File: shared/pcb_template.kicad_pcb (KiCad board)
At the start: 2 copper layers, 100 x 50 mm, 8 parts, among them J1 WEST TOP, J2 WEST BOT, J3 EAST TOP, J4 EAST BOT, X2 HOLE, X3 HOLE, X4 HOLE, X5 HOLE

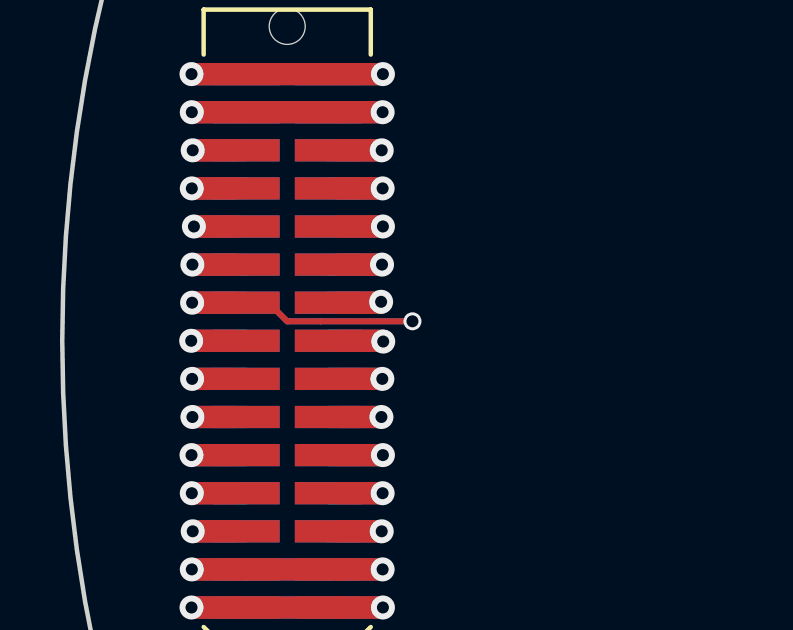
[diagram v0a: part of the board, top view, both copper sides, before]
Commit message: added pcb template
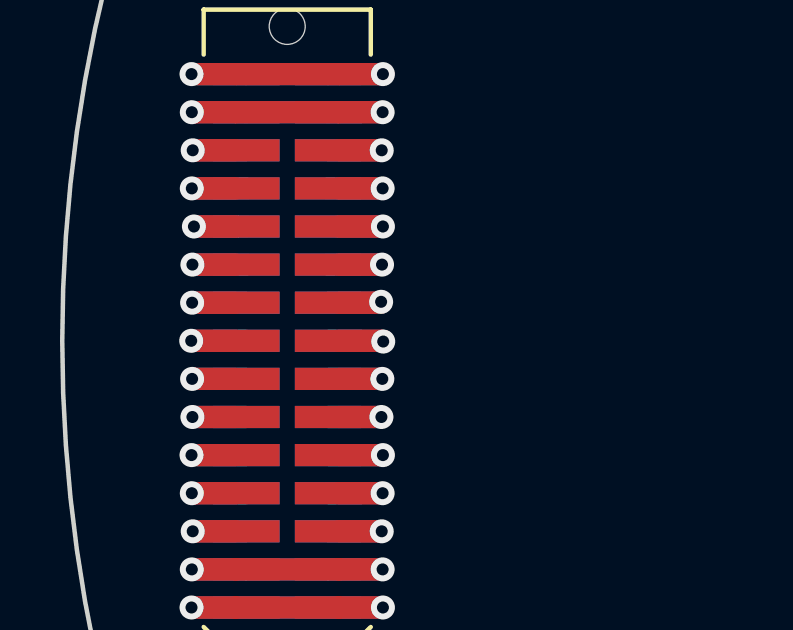
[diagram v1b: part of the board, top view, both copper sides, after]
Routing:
- net 3v3: track 16.3 -> 6.19 mm, vias 2 -> 1
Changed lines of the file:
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@@
     (thickness 1.6)
     (drawings 9)
-    (tracks 206)
+    (tracks 198)
     (zones 0)
     (modules 8)
@@
   (via (at 139.31 91.11) (size 0.8) (drill 0.4) (layers F.Cu B.Cu) (net 1))
   (segment (start 140.785 91.11) (end 139.31 91.11) (width 0.74) (layer F.Cu) (net 1))
-  (via (at 61.67499 99.35001) (size 0.6) (drill 0.4) (layers F.Cu B.Cu) (net 2))
-  (segment (start 58.608184 99.35001) (end 61.67499 99.35001) (width 0.2) (layer B.Cu) (net 2))
-  (segment (start 57.554999 99.350001) (end 58.608175 99.350001) (width 0.2) (layer B.Cu) (net 2))
-  (segment (start 58.608175 99.350001) (end 58.608184 99.35001) (width 0.2) (layer B.Cu) (net 2))
-  (segment (start 57.495 99.35) (end 57.554999 99.350001) (width 0.2) (layer B.Cu) (net 2))
   (segment (start 56.135 98.73) (end 56.875 98.73) (width 0.2) (layer B.Cu) (net 2))
-  (segment (start 56.875 98.73) (end 57.495 99.35) (width 0.2) (layer B.Cu) (net 2))
-  (segment (start 56.88 98.73) (end 57.500001 99.350001) (width 0.2) (layer F.Cu) (net 2))
-  (segment (start 57.500001 99.350001) (end 61.674999 99.350001) (width 0.2) (layer F.Cu) (net 2))
   (segment (start 55.785 98.73) (end 56.88 98.73) (width 0.2) (layer F.Cu) (net 2))
   (segment (start 55.785 98.73) (end 56.875 98.73) (width 0.2) (layer F.Cu) (net 2))
